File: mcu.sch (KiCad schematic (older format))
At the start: 76 parts, among them J10 JTAG, J11 esp32L, J12 esp32B, J13 esp32R, J2 SPI1, J3 uSD, J4 I2C1, J5 serial1, J6 serial2, J7 touch interface, J8 LCD 4.3, J9 EXT_IOS, Q1 ZXMN2F30FH, Q2 ZXMN2F30FH, Q3 ZXMN2F30FH, SW1 reset, SW7 on, U3 AT25SF641, U5 STM32F750Z8, U6 MP3302DJ-LF-P, U7 ESP32-WROOM-32, Y1 25MHz, Y2 32.768 kHz

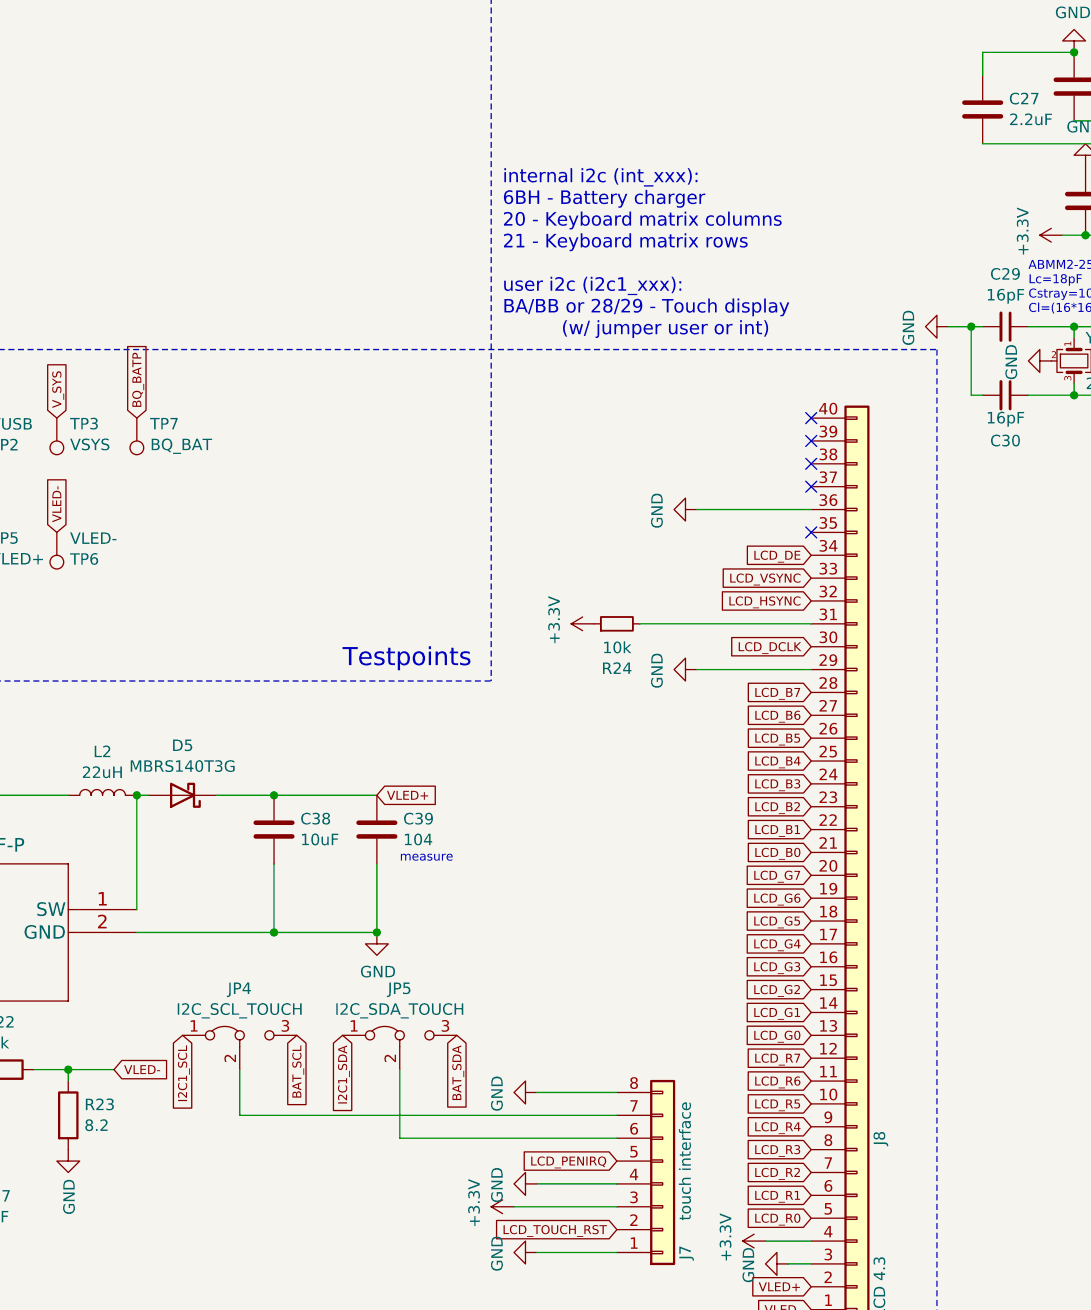
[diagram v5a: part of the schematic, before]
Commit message: No jumper finally
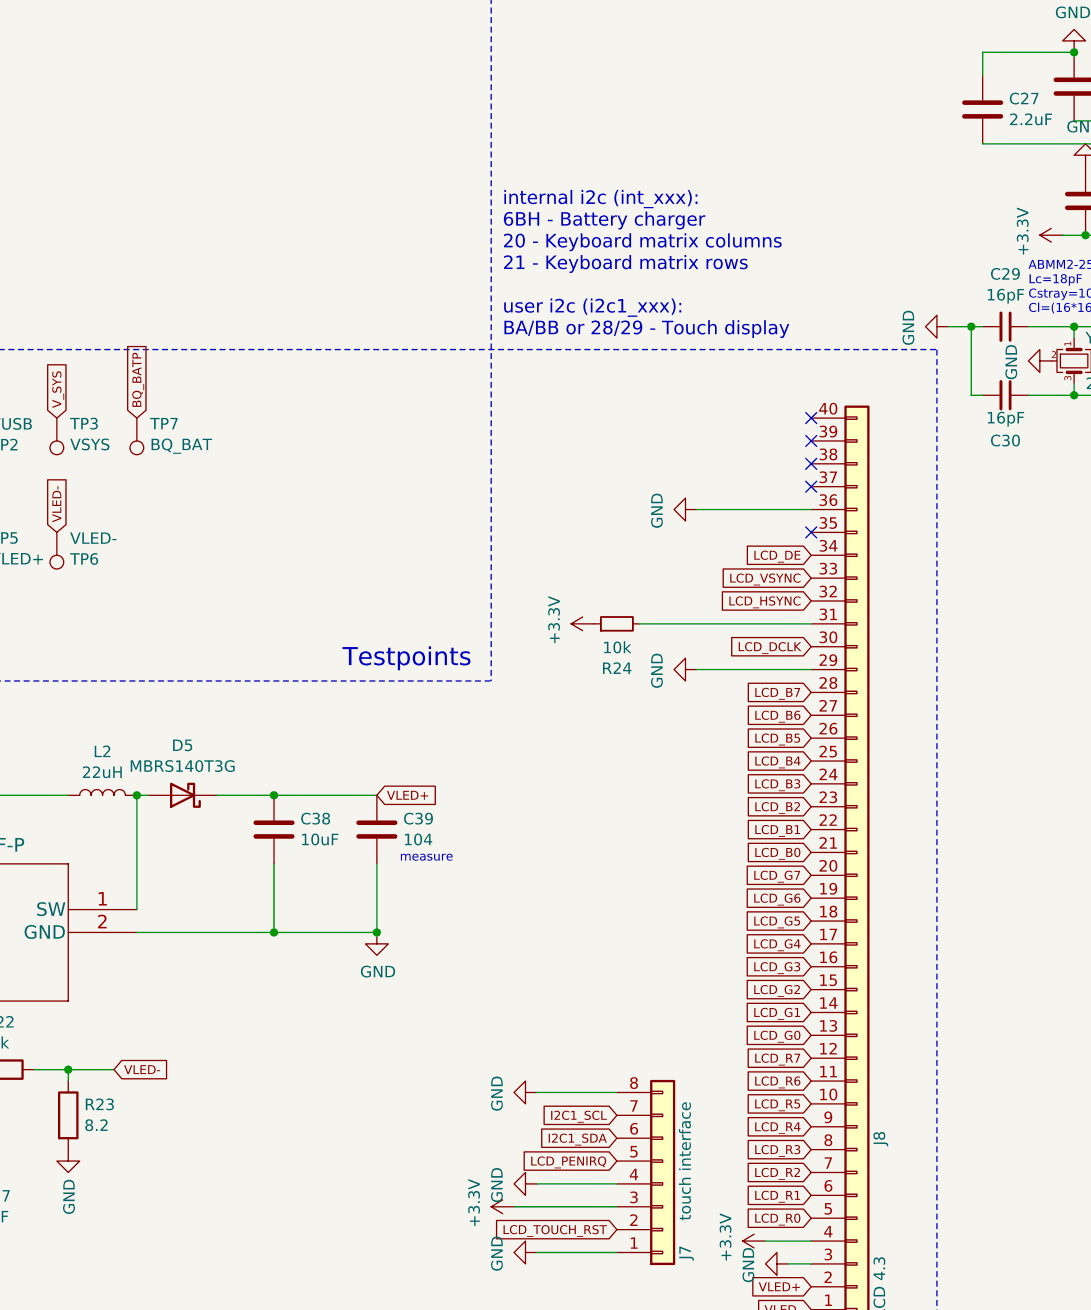
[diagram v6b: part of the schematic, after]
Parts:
- removed JP4: I2C_SCL_TOUCH, Jumper:SolderJumper-3_P1.3mm_Bridged2Bar12_Pad1.0x1.5mm_NumberLabels, symbol Jumper:Jumper_3_Bridged12
- removed JP5: I2C_SDA_TOUCH, Jumper:SolderJumper-3_P1.3mm_Bridged2Bar12_Pad1.0x1.5mm_NumberLabels, symbol Jumper:Jumper_3_Bridged12
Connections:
- net I2C1_SCL: now also J7.7 (Pin_7)
- net I2C1_SDA: now also J7.6 (Pin_6)
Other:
- note added: "internal i2c (int_xxx):\n6BH - Battery charger\n20 - Keyboard matrix columns\n21 - Keyboard matrix rows\n\nuser i2c (i2c1_xxx):\nBA/BB or 28/29 - Touch display\n"
- note removed: "internal i2c (int_xxx):\n6BH - Battery charger\n20 - Keyboard matrix columns\n21 - Keyboard matrix rows\n\nuser i2c (i2c1_xxx):\nBA/BB or 28/29 - Touch display\n (w/ jumper user or int)"
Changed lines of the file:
@@
 $EndComp
 NoConn ~ 12750 6350
-Text GLabel 8250 6550 3    39   Input ~ 0
+Text GLabel 10150 6900 0    39   Input ~ 0
 I2C1_SCL
-Text GLabel 8950 6550 3    39   Input ~ 0
+Text GLabel 10150 7000 0    39   Input ~ 0
 I2C1_SDA
 $Comp
@@
 KB_WAKEUP
 Text Notes 9650 3500 0    59   ~ 0
-internal i2c (int_xxx):\n6BH - Battery charger\n20 - Keyboard matrix columns\n21 - Keyboard matrix rows\n\nuser i2c (i2c1_xxx):\nBA/BB or 28/29 - Touch display\n          (w/ jumper user or int)
+internal i2c (int_xxx):\n6BH - Battery charger\n20 - Keyboard matrix columns\n21 - Keyboard matrix rows\n\nuser i2c (i2c1_xxx):\nBA/BB or 28/29 - Touch display\n
 $Comp
 L power:+3.3V #PWR0111
@@
 Wire Wire Line
 	6250 6000 5900 6000
-$Comp
-L Jumper:Jumper_3_Bridged12 JP4
-U 1 1 6188C10F
-P 8500 6550
-F 0 "JP4" H 8500 6754 50  0000 C CNN
-F 1 "I2C_SCL_TOUCH" H 8500 6663 50  0000 C CNN
-F 2 "Jumper:SolderJumper-3_P1.3mm_Bridged2Bar12_Pad1.0x1.5mm_NumberLabels" H 8500 6550 50  0001 C CNN
-F 3 "~" H 8500 6550 50  0001 C CNN
-	1    8500 6550
-	1    0    0    -1
-$EndComp
-$Comp
-L Jumper:Jumper_3_Bridged12 JP5
-U 1 1 6188CE27
-P 9200 6550
-F 0 "JP5" H 9200 6754 50  0000 C CNN
-F 1 "I2C_SDA_TOUCH" H 9200 6663 50  0000 C CNN
-F 2 "Jumper:SolderJumper-3_P1.3mm_Bridged2Bar12_Pad1.0x1.5mm_NumberLabels" H 9200 6550 50  0001 C CNN
-F 3 "~" H 9200 6550 50  0001 C CNN
-	1    9200 6550
-	1    0    0    -1
-$EndComp
-Wire Wire Line
-	8500 6700 8500 6900
-Wire Wire Line
-	8500 6900 10150 6900
-Wire Wire Line
-	9200 6700 9200 7000
-Wire Wire Line
-	9200 7000 10150 7000
-Text GLabel 8750 6550 3    39   Input ~ 0
-BAT_SCL
-Text GLabel 9450 6550 3    39   Input ~ 0
-BAT_SDA
 $EndSCHEMATC

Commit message: fix and switch
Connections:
- net BAT_SCL is gone; now on net INT_SCL: R11.2
- net BAT_SDA is gone; now on net INT_SDA: R10.2
- net I2C1_SCL: no longer J7.7 (Pin_7)
- net I2C1_SDA: no longer J7.6 (Pin_6)
- net INT_SCL: now also J7.7 (Pin_7)
- net INT_SDA: now also J7.6 (Pin_6)
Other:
- note added: "internal i2c (int_xxx):\n6BH - Battery charger\n20 - Keyboard matrix columns\n21 - Keyboard matrix rows\nBA/BB or 28/29 - Touch display\n"
- note removed: "internal i2c (int_xxx):\n6BH - Battery charger\n20 - Keyboard matrix columns\n21 - Keyboard matrix rows\n\nuser i2c (i2c1_xxx):\nBA/BB or 28/29 - Touch display\n"
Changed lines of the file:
@@
 $EndComp
 Text GLabel 12150 1300 3    39   Input ~ 0
-BAT_SDA
+INT_SDA
 Text GLabel 12450 1300 3    39   Input ~ 0
-BAT_SCL
+INT_SCL
 $Comp
 L Device:R R11
@@
 NoConn ~ 12750 6350
 Text GLabel 10150 6900 0    39   Input ~ 0
-I2C1_SCL
+INT_SCL
 Text GLabel 10150 7000 0    39   Input ~ 0
-I2C1_SDA
+INT_SDA
 $Comp
 L power:GND #PWR018
@@
 KB_WAKEUP
 Text Notes 9650 3500 0    59   ~ 0
-internal i2c (int_xxx):\n6BH - Battery charger\n20 - Keyboard matrix columns\n21 - Keyboard matrix rows\n\nuser i2c (i2c1_xxx):\nBA/BB or 28/29 - Touch display\n
+internal i2c (int_xxx):\n6BH - Battery charger\n20 - Keyboard matrix columns\n21 - Keyboard matrix rows\nBA/BB or 28/29 - Touch display\n
 $Comp
 L power:+3.3V #PWR0111
